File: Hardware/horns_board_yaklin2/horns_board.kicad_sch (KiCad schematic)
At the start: 15 parts, among them J1 Power In, J2 Horn Ctrl, J3 Horn Out 2, J4 Horn Out 1, Q1 NMOS

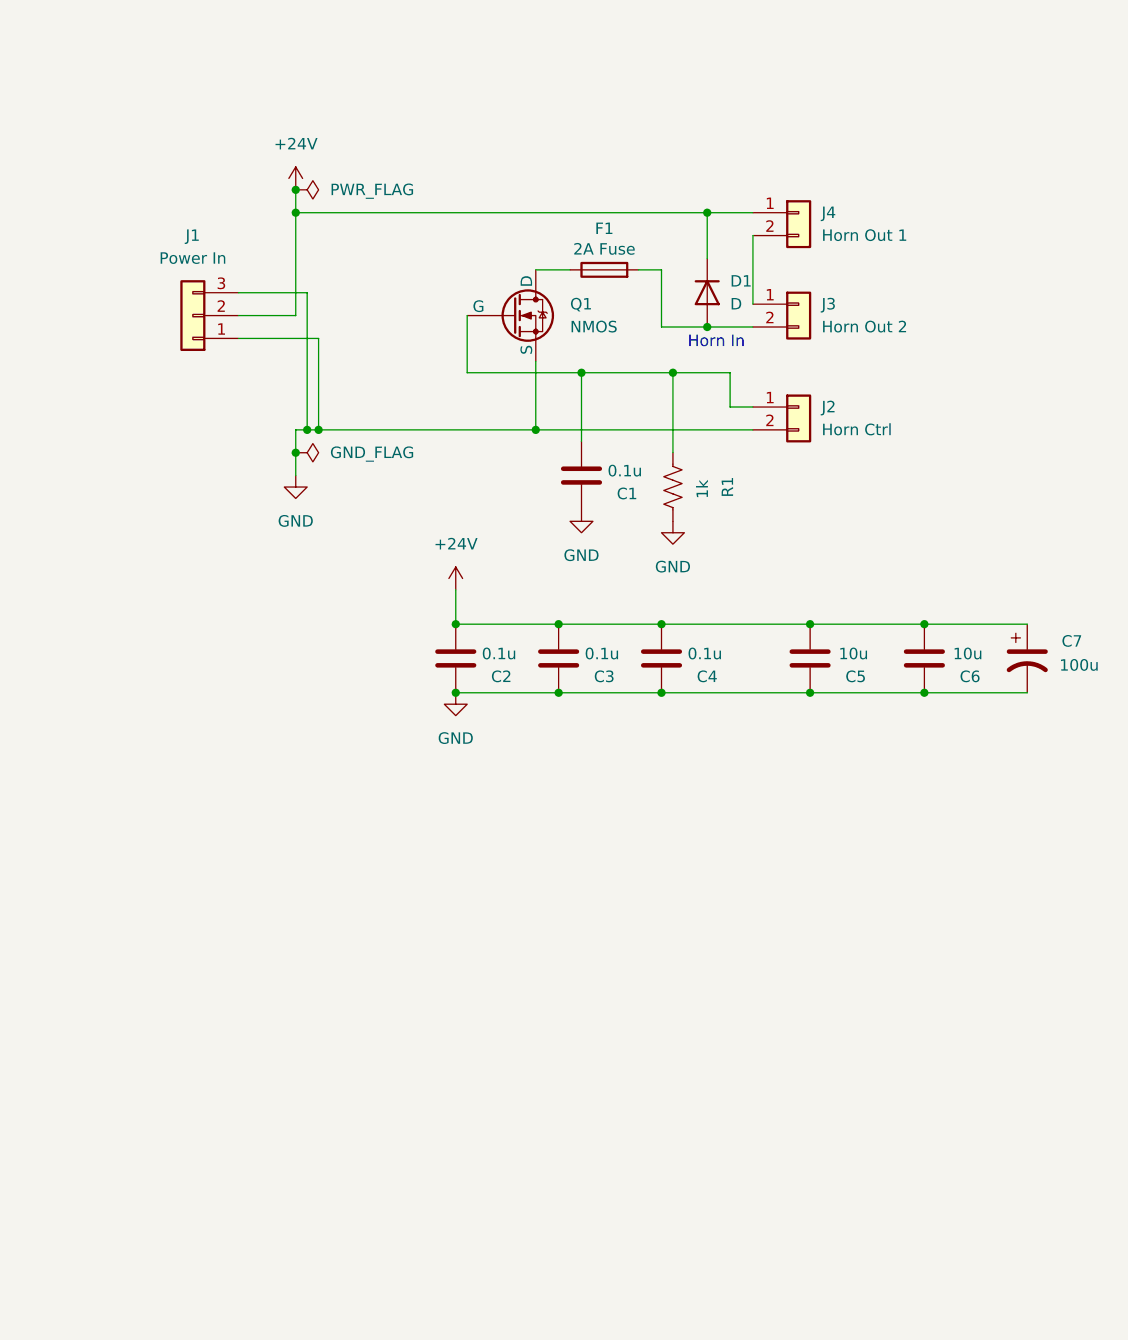
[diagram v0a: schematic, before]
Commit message: Updated according to comments
Split schematic into multiple modules instead of a single loop.
Replaced Molex kk254 connectors with micro fit and rerouted the traces accordingly.
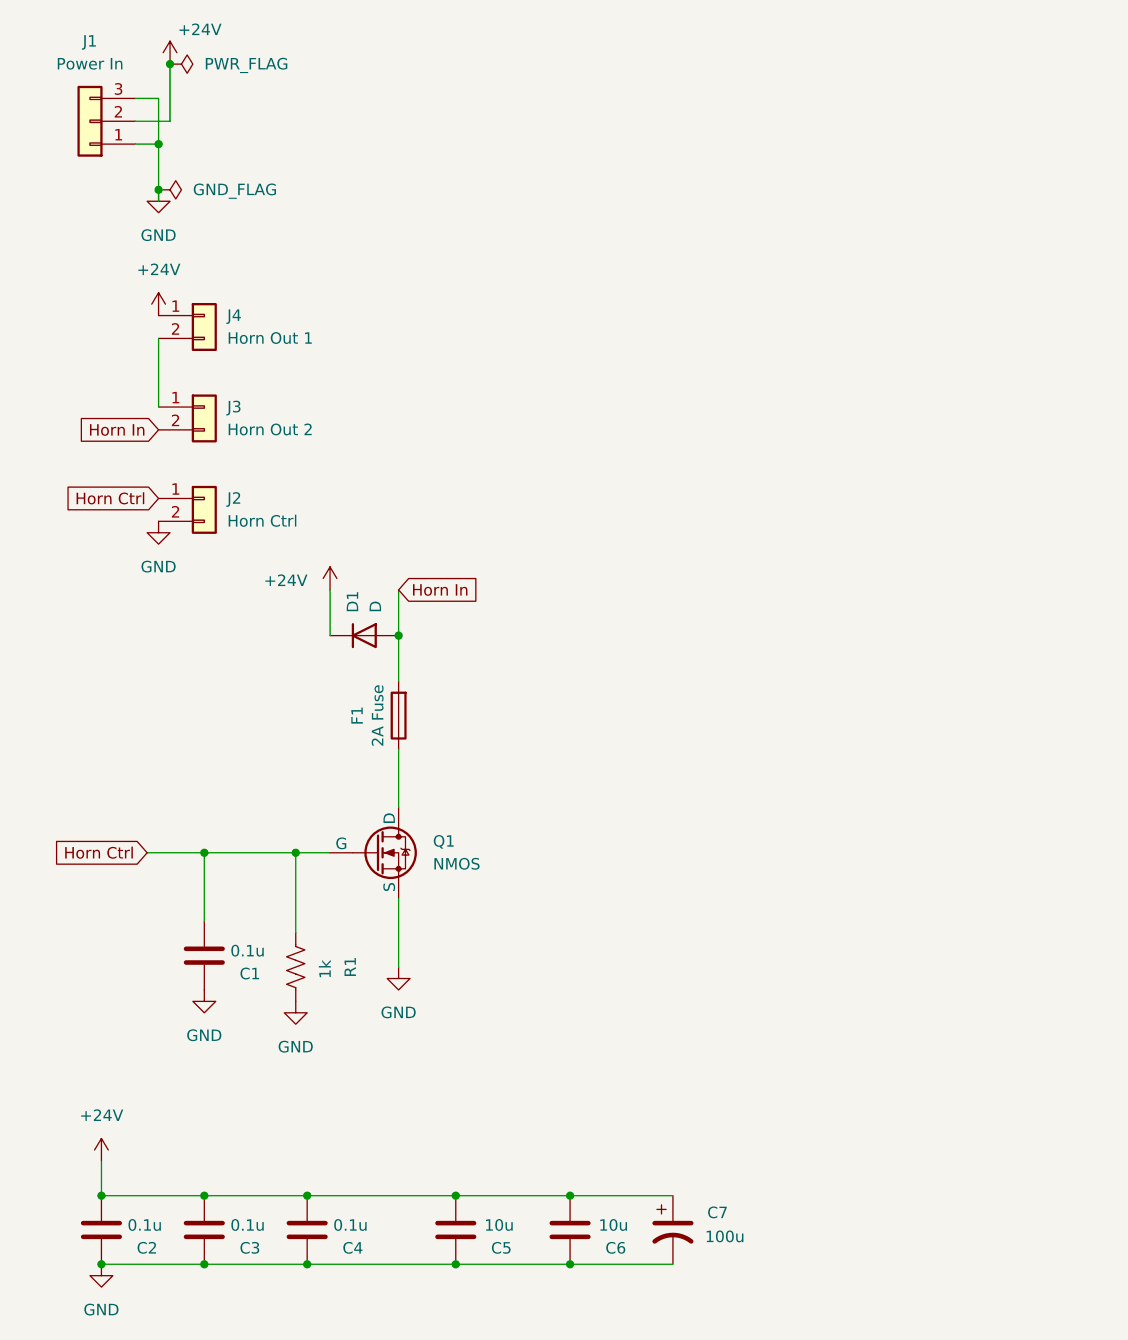
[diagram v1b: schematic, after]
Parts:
- J1: footprint Connector_Molex:Molex_KK-254_AE-6410-03A_1x03_P2.54mm_Vertical -> Connector_Molex:Molex_Micro-Fit_3.0_43650-0315_1x03_P3.00mm_Vertical
- J2, J3, J4: footprint Connector_Molex:Molex_KK-254_AE-6410-02A_1x02_P2.54mm_Vertical -> Connector_Molex:Molex_Micro-Fit_3.0_43650-0215_1x02_P3.00mm_Vertical
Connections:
- net Horn Ctrl: now reaches C1.2, J2.1 (Pin_1), Q1.2 (G), R1.2
- net Horn In: now reaches D1.2 (A), F1.2, J3.2 (Pin_2)
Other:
- note removed: "Horn In"
- moved on the sheet: C1, C2, C3, C4, C5, C6, C7, D1, F1, J1, J2, J3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
